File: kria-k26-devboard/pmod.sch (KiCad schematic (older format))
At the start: 6 parts

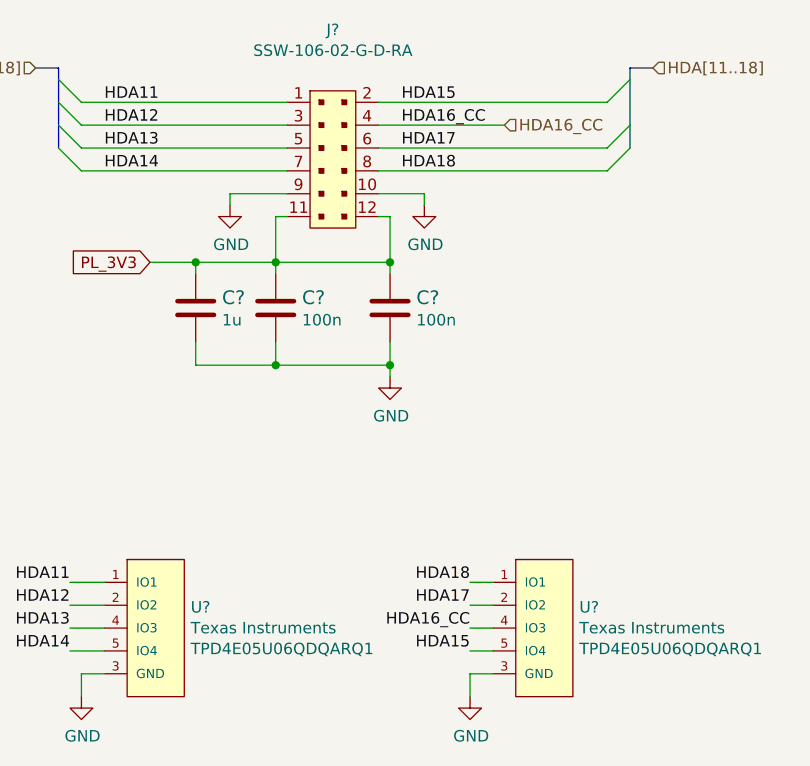
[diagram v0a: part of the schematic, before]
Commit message: Added second ETH interface, connect POE PSE
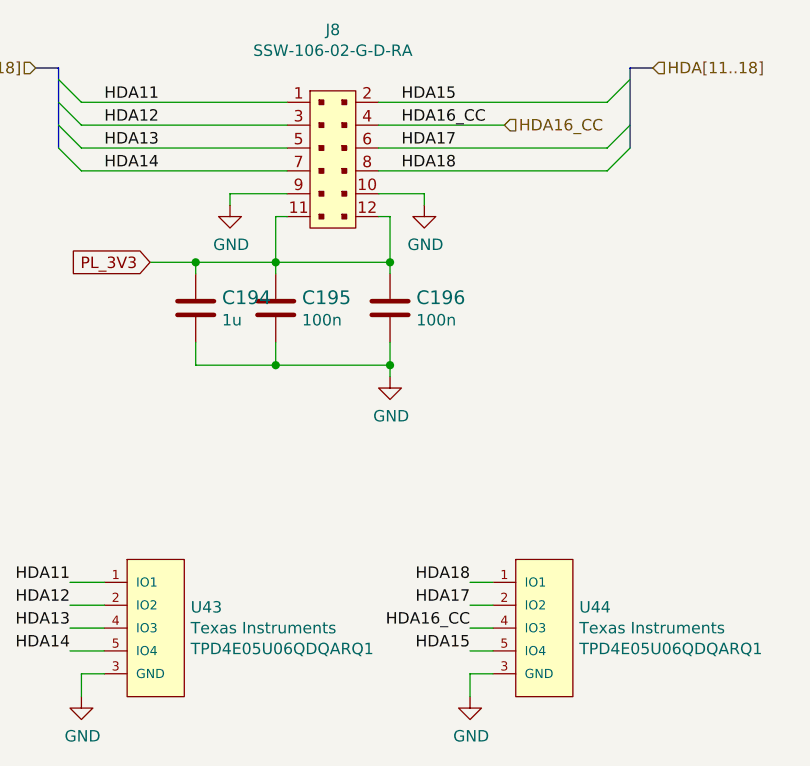
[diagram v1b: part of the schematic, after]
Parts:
- gave numbers to parts that had none: 6
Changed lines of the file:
@@
 $EndDescr
 $Comp
-L antmicroTVSDiodes:TPD4E05U06QDQARQ1 U?
+L antmicroTVSDiodes:TPD4E05U06QDQARQ1 U43
 U 1 1 6498DC0A
 P 4600 5050
-F 0 "U?" H 4928 5141 50  0000 L CNN
+F 0 "U43" H 4928 5141 50  0000 L CNN
 F 1 "TPD4E05U06QDQARQ1" H 4650 4650 50  0001 L CNN
 F 2 "antmicro-footprints:TPD4E05U06QDQARQ1" H 4650 5500 50  0001 L CNN
@@
 $EndComp
 $Comp
-L antmicroRectangularConnectorsHeadersFemalePins:SSW-106-02-G-D-RA J?
+L antmicroRectangularConnectorsHeadersFemalePins:SSW-106-02-G-D-RA J8
 U 1 1 649925B1
 P 5550 3000
-F 0 "J?" H 5550 3567 50  0000 C CNN
+F 0 "J8" H 5550 3567 50  0000 C CNN
 F 1 "SSW-106-02-G-D-RA" H 5550 3476 50  0000 C CNN
 F 2 "antmicro-footprints:SAMTEC_SSW-106-02-G-D-RA" H 5150 3550 50  0001 L BNN
@@
 	5100 3150 5100 3200
 $Comp
-L power:GND #PWR?
+L power:GND #PWR0329
 U 1 1 649A6690
 P 4450 5350
-F 0 "#PWR?" H 4450 5100 50  0001 C CNN
+F 0 "#PWR0329" H 4450 5100 50  0001 C CNN
 F 1 "GND" H 4455 5177 50  0000 C CNN
 F 2 "" H 4450 5350 50  0001 C CNN
@@
 	4450 5250 4550 5250
 $Comp
-L power:GND #PWR?
+L power:GND #PWR0330
 U 1 1 649A6F75
 P 5100 3200
-F 0 "#PWR?" H 5100 2950 50  0001 C CNN
+F 0 "#PWR0330" H 5100 2950 50  0001 C CNN
 F 1 "GND" H 5105 3027 50  0000 C CNN
 F 2 "" H 5100 3200 50  0001 C CNN
@@
 $EndComp
 $Comp
-L power:GND #PWR?
+L power:GND #PWR0331
 U 1 1 649A7323
 P 5950 3200
-F 0 "#PWR?" H 5950 2950 50  0001 C CNN
+F 0 "#PWR0331" H 5950 2950 50  0001 C CNN
 F 1 "GND" H 5955 3027 50  0000 C CNN
 F 2 "" H 5950 3200 50  0001 C CNN
@@
 	6250 5050 6150 5050
 $Comp
-L antmicroTVSDiodes:TPD4E05U06QDQARQ1 U?
+L antmicroTVSDiodes:TPD4E05U06QDQARQ1 U44
 U 1 1 649B0170
 P 6300 5050
-F 0 "U?" H 6628 5141 50  0000 L CNN
+F 0 "U44" H 6628 5141 50  0000 L CNN
 F 1 "TPD4E05U06QDQARQ1" H 6350 4650 50  0001 L CNN
 F 2 "antmicro-footprints:TPD4E05U06QDQARQ1" H 6350 5500 50  0001 L CNN
@@
 	6150 5150 6250 5150
 $Comp
-L power:GND #PWR?
+L power:GND #PWR0332
 U 1 1 649B2E10
 P 6150 5350
-F 0 "#PWR?" H 6150 5100 50  0001 C CNN
+F 0 "#PWR0332" H 6150 5100 50  0001 C CNN
 F 1 "GND" H 6155 5177 50  0000 C CNN
 F 2 "" H 6150 5350 50  0001 C CNN
@@
 PL_3V3
 $Comp
-L antmicroCapacitors0402:C_100n_0402 C?
+L antmicroCapacitors0402:C_100n_0402 C195
 U 1 1 649C2025
 P 5300 3650
-F 0 "C?" H 5415 3695 60  0000 L CNN
+F 0 "C195" H 5415 3695 60  0000 L CNN
 F 1 "C_100n_0402" H 5300 3500 60  0001 C CNN
 F 2 "antmicro-footprints:0402-cap" H 5500 3850 60  0001 L CNN
@@
 $EndComp
 $Comp
-L antmicroCapacitors0402:C_100n_0402 C?
+L antmicroCapacitors0402:C_100n_0402 C196
 U 1 1 649C25C6
 P 5800 3650
-F 0 "C?" H 5915 3695 60  0000 L CNN
+F 0 "C196" H 5915 3695 60  0000 L CNN
 F 1 "C_100n_0402" H 5800 3500 60  0001 C CNN
 F 2 "antmicro-footprints:0402-cap" H 6000 3850 60  0001 L CNN
@@
 $EndComp
 $Comp
-L antmicroCapacitors0402:C_1u_0402 C?
+L antmicroCapacitors0402:C_1u_0402 C194
 U 1 1 649C4ADC
 P 4950 3650
-F 0 "C?" H 5065 3695 60  0000 L CNN
+F 0 "C194" H 5065 3695 60  0000 L CNN
 F 1 "C_1u_0402" H 4950 3500 60  0001 C CNN
 F 2 "antmicro-footprints:0402-cap" H 5150 3850 60  0001 L CNN
@@
 	4950 3800 4950 3900
 $Comp
-L power:GND #PWR?
+L power:GND #PWR0333
 U 1 1 649DA63B
 P 5800 3950
-F 0 "#PWR?" H 5800 3700 50  0001 C CNN
+F 0 "#PWR0333" H 5800 3700 50  0001 C CNN
 F 1 "GND" H 5805 3777 50  0000 C CNN
 F 2 "" H 5800 3950 50  0001 C CNN

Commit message: Finished tidying up the schematic
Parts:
- added D?: ESD9L5.0ST5G, antmicro-footprints:DIOM1006X40N, symbol antmicroTVSDiodes:ESD9L5.0ST5G
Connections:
- wire segments 40 -> 44
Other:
- note added: "PMOD"
- moved on the sheet: C194
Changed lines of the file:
@@
 $Descr A4 11693 8268
 encoding utf-8
-Sheet 16 19
+Sheet 8 19
 Title ""
 Date ""
@@
 Wire Wire Line
 	5350 3250 5300 3250
-Text GLabel 4750 3450 0    50   Input ~ 0
+Text GLabel 3900 3450 0    50   Input ~ 0
 PL_3V3
 $Comp
@@
 L antmicroCapacitors0402:C_1u_0402 C194
 U 1 1 649C4ADC
-P 4950 3650
-F 0 "C194" H 5065 3695 60  0000 L CNN
-F 1 "C_1u_0402" H 4950 3500 60  0001 C CNN
-F 2 "antmicro-footprints:0402-cap" H 5150 3850 60  0001 L CNN
-F 3 "" H 4950 3650 50  0001 C CNN
-F 4 "TDK" H 5150 4050 60  0001 L CNN "Manufacturer"
-F 5 "C1005X6S1A105K050BC" H 5150 3950 60  0001 L CNN "MPN"
-F 6 "1u" H 5065 3597 50  0000 L CNN "Val"
-	1    4950 3650
-	1    0    0    -1
-$EndComp
-Wire Wire Line
-	4950 3500 4950 3450
+P 4800 3650
+F 0 "C194" H 4915 3695 60  0000 L CNN
+F 1 "C_1u_0402" H 4800 3500 60  0001 C CNN
+F 2 "antmicro-footprints:0402-cap" H 5000 3850 60  0001 L CNN
+F 3 "" H 4800 3650 50  0001 C CNN
+F 4 "TDK" H 5000 4050 60  0001 L CNN "Manufacturer"
+F 5 "C1005X6S1A105K050BC" H 5000 3950 60  0001 L CNN "MPN"
+F 6 "1u" H 4915 3597 50  0000 L CNN "Val"
+	1    4800 3650
+	1    0    0    -1
+$EndComp
+Wire Wire Line
+	4800 3500 4800 3450
 Wire Wire Line
 	5750 3250 5800 3250
 Wire Wire Line
 	5300 3250 5300 3450
-Wire Wire Line
-	4750 3450 4950 3450
-Connection ~ 4950 3450
-Wire Wire Line
-	4950 3800 4950 3900
+Connection ~ 4800 3450
 $Comp
 L power:GND #PWR0333
 U 1 1 649DA63B
-P 5800 3950
-F 0 "#PWR0333" H 5800 3700 50  0001 C CNN
-F 1 "GND" H 5805 3777 50  0000 C CNN
-F 2 "" H 5800 3950 50  0001 C CNN
-F 3 "" H 5800 3950 50  0001 C CNN
-	1    5800 3950
+P 5800 4150
+F 0 "#PWR0333" H 5800 3900 50  0001 C CNN
+F 1 "GND" H 5805 3977 50  0000 C CNN
+F 2 "" H 5800 4150 50  0001 C CNN
+F 3 "" H 5800 4150 50  0001 C CNN
+	1    5800 4150
 	1    0    0    -1
 $EndComp
@@
 	5800 3450 5800 3500
 Wire Wire Line
-	5800 3900 5800 3800
-Wire Wire Line
 	5300 3500 5300 3450
-Wire Wire Line
-	5300 3800 5300 3900
-Connection ~ 5300 3900
-Wire Wire Line
-	5300 3900 5800 3900
-Wire Wire Line
-	5800 3950 5800 3900
-Connection ~ 5800 3900
-Wire Wire Line
-	4950 3900 5300 3900
-Wire Wire Line
-	4950 3450 5300 3450
+Connection ~ 5300 4100
+Wire Wire Line
+	5300 4100 5800 4100
+Wire Wire Line
+	4800 4100 5300 4100
+Wire Wire Line
+	4800 3450 5300 3450
+Text Notes 550  750  0    100  ~ 20
+PMOD
+$Comp
+L antmicroTVSDiodes:ESD9L5.0ST5G D?
+U 1 1 69767A1C
+P 4050 3750
+F 0 "D?" V 4096 3650 50  0000 R CNN
+F 1 "ESD9L5.0ST5G" V 4005 3650 50  0000 R CNN
+F 2 "antmicro-footprints:DIOM1006X40N" H 3800 3950 50  0001 C CNN
+F 3 "https://www.farnell.com/datasheets/2353986.pdf" H 4050 3750 50  0001 C CNN
+F 4 "ESD9L5.0ST5G" H 3750 4000 50  0001 C CNN "MPN"
+F 5 "ONSEMI" H 4200 4000 50  0001 C CNN "Manufacturer"
+	1    4050 3750
+	0    -1   -1   0
+$EndComp
+Wire Wire Line
+	3900 3450 4050 3450
+Wire Wire Line
+	4800 4100 4050 4100
+Wire Wire Line
+	4050 4100 4050 4000
+Wire Wire Line
+	4050 3500 4050 3450
+Connection ~ 4050 3450
+Wire Wire Line
+	4050 3450 4800 3450
+Wire Wire Line
+	4800 3800 4800 4100
+Wire Wire Line
+	5800 4150 5800 4100
+Wire Wire Line
+	5800 3800 5800 4100
+Connection ~ 5800 4100
+Wire Wire Line
+	5300 3800 5300 4100
+Connection ~ 4800 4100
 Wire Bus Line
 	6850 2600 6850 2950

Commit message: Initial placement of power supply
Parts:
- removed D?: ESD9L5.0ST5G, antmicro-footprints:DIOM1006X40N, symbol antmicroTVSDiodes:ESD9L5.0ST5G
- added D3: PTVS5V0Z1USKPYL, antmicro-footprints:SOD-964, symbol antmicroTVSDiodes:PTVS5V0Z1USKPYL
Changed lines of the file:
@@
 Text Notes 550  750  0    100  ~ 20
 PMOD
-$Comp
-L antmicroTVSDiodes:ESD9L5.0ST5G D?
-U 1 1 69767A1C
-P 4050 3750
-F 0 "D?" V 4096 3650 50  0000 R CNN
-F 1 "ESD9L5.0ST5G" V 4005 3650 50  0000 R CNN
-F 2 "antmicro-footprints:DIOM1006X40N" H 3800 3950 50  0001 C CNN
-F 3 "https://www.farnell.com/datasheets/2353986.pdf" H 4050 3750 50  0001 C CNN
-F 4 "ESD9L5.0ST5G" H 3750 4000 50  0001 C CNN "MPN"
-F 5 "ONSEMI" H 4200 4000 50  0001 C CNN "Manufacturer"
-	1    4050 3750
-	0    -1   -1   0
-$EndComp
 Wire Wire Line
 	3900 3450 4050 3450
 Wire Wire Line
 	4800 4100 4050 4100
-Wire Wire Line
-	4050 4100 4050 4000
-Wire Wire Line
-	4050 3500 4050 3450
 Connection ~ 4050 3450
 Wire Wire Line
@@
 	5300 3800 5300 4100
 Connection ~ 4800 4100
+$Comp
+L antmicroTVSDiodes:PTVS5V0Z1USKPYL D3
+U 1 1 69B7F430
+P 4050 3750
+F 0 "D3" V 4103 3622 60  0000 R CNN
+F 1 "PTVS5V0Z1USKPYL" H 4250 3950 60  0000 R CNN
+F 2 "antmicro-footprints:SOD-964" H 4250 3950 60  0001 L CNN
+F 3 "https://pl.mouser.com/datasheet/2/916/PTVS5V0Z1USKP-1600477.pdf" H 4250 4050 60  0001 L CNN
+F 4 "Nexperia" H 4250 4850 60  0001 L CNN "Manufacturer"
+F 5 "PTVS5V0Z1USKPYL" H 4250 4250 60  0001 L CNN "MPN"
+	1    4050 3750
+	0    -1   -1   0
+$EndComp
+Wire Wire Line
+	4050 3450 4050 3550
+Wire Wire Line
+	4050 3950 4050 4100
 Wire Bus Line
 	6850 2600 6850 2950

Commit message: Progress in PCB placement
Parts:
- renumbered C194 to C39, C195 to C40, C196 to C41, J8 to J4, U43 to U12, U44 to U13
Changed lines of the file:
@@
 $EndDescr
 $Comp
-L antmicroTVSDiodes:TPD4E05U06QDQARQ1 U43
+L antmicroTVSDiodes:TPD4E05U06QDQARQ1 U12
 U 1 1 6498DC0A
 P 4600 5050
-F 0 "U43" H 4928 5141 50  0000 L CNN
+F 0 "U12" H 4928 5141 50  0000 L CNN
 F 1 "TPD4E05U06QDQARQ1" H 4650 4650 50  0001 L CNN
 F 2 "antmicro-footprints:TPD4E05U06QDQARQ1" H 4650 5500 50  0001 L CNN
@@
 $EndComp
 $Comp
-L antmicroRectangularConnectorsHeadersFemalePins:SSW-106-02-G-D-RA J8
+L antmicroRectangularConnectorsHeadersFemalePins:SSW-106-02-G-D-RA J4
 U 1 1 649925B1
 P 5550 3000
-F 0 "J8" H 5550 3567 50  0000 C CNN
+F 0 "J4" H 5550 3567 50  0000 C CNN
 F 1 "SSW-106-02-G-D-RA" H 5550 3476 50  0000 C CNN
 F 2 "antmicro-footprints:SAMTEC_SSW-106-02-G-D-RA" H 5150 3550 50  0001 L BNN
@@
 	5100 3150 5100 3200
 $Comp
-L power:GND #PWR0329
+L power:GND #PWR062
 U 1 1 649A6690
 P 4450 5350
-F 0 "#PWR0329" H 4450 5100 50  0001 C CNN
+F 0 "#PWR062" H 4450 5100 50  0001 C CNN
 F 1 "GND" H 4455 5177 50  0000 C CNN
 F 2 "" H 4450 5350 50  0001 C CNN
@@
 	4450 5250 4550 5250
 $Comp
-L power:GND #PWR0330
+L power:GND #PWR063
 U 1 1 649A6F75
 P 5100 3200
-F 0 "#PWR0330" H 5100 2950 50  0001 C CNN
+F 0 "#PWR063" H 5100 2950 50  0001 C CNN
 F 1 "GND" H 5105 3027 50  0000 C CNN
 F 2 "" H 5100 3200 50  0001 C CNN
@@
 $EndComp
 $Comp
-L power:GND #PWR0331
+L power:GND #PWR065
 U 1 1 649A7323
 P 5950 3200
-F 0 "#PWR0331" H 5950 2950 50  0001 C CNN
+F 0 "#PWR065" H 5950 2950 50  0001 C CNN
 F 1 "GND" H 5955 3027 50  0000 C CNN
 F 2 "" H 5950 3200 50  0001 C CNN
@@
 	6250 5050 6150 5050
 $Comp
-L antmicroTVSDiodes:TPD4E05U06QDQARQ1 U44
+L antmicroTVSDiodes:TPD4E05U06QDQARQ1 U13
 U 1 1 649B0170
 P 6300 5050
-F 0 "U44" H 6628 5141 50  0000 L CNN
+F 0 "U13" H 6628 5141 50  0000 L CNN
 F 1 "TPD4E05U06QDQARQ1" H 6350 4650 50  0001 L CNN
 F 2 "antmicro-footprints:TPD4E05U06QDQARQ1" H 6350 5500 50  0001 L CNN
@@
 	6150 5150 6250 5150
 $Comp
-L power:GND #PWR0332
+L power:GND #PWR066
 U 1 1 649B2E10
 P 6150 5350
-F 0 "#PWR0332" H 6150 5100 50  0001 C CNN
+F 0 "#PWR066" H 6150 5100 50  0001 C CNN
 F 1 "GND" H 6155 5177 50  0000 C CNN
 F 2 "" H 6150 5350 50  0001 C CNN
@@
 PL_3V3
 $Comp
-L antmicroCapacitors0402:C_100n_0402 C195
+L antmicroCapacitors0402:C_100n_0402 C40
 U 1 1 649C2025
 P 5300 3650
-F 0 "C195" H 5415 3695 60  0000 L CNN
+F 0 "C40" H 5415 3695 60  0000 L CNN
 F 1 "C_100n_0402" H 5300 3500 60  0001 C CNN
 F 2 "antmicro-footprints:0402-cap" H 5500 3850 60  0001 L CNN
@@
 $EndComp
 $Comp
-L antmicroCapacitors0402:C_100n_0402 C196
+L antmicroCapacitors0402:C_100n_0402 C41
 U 1 1 649C25C6
 P 5800 3650
-F 0 "C196" H 5915 3695 60  0000 L CNN
+F 0 "C41" H 5915 3695 60  0000 L CNN
 F 1 "C_100n_0402" H 5800 3500 60  0001 C CNN
 F 2 "antmicro-footprints:0402-cap" H 6000 3850 60  0001 L CNN
@@
 $EndComp
 $Comp
-L antmicroCapacitors0402:C_1u_0402 C194
+L antmicroCapacitors0402:C_1u_0402 C39
 U 1 1 649C4ADC
 P 4800 3650
-F 0 "C194" H 4915 3695 60  0000 L CNN
+F 0 "C39" H 4915 3695 60  0000 L CNN
 F 1 "C_1u_0402" H 4800 3500 60  0001 C CNN
 F 2 "antmicro-footprints:0402-cap" H 5000 3850 60  0001 L CNN
@@
 Connection ~ 4800 3450
 $Comp
-L power:GND #PWR0333
+L power:GND #PWR064
 U 1 1 649DA63B
 P 5800 4150
-F 0 "#PWR0333" H 5800 3900 50  0001 C CNN
+F 0 "#PWR064" H 5800 3900 50  0001 C CNN
 F 1 "GND" H 5805 3977 50  0000 C CNN
 F 2 "" H 5800 4150 50  0001 C CNN

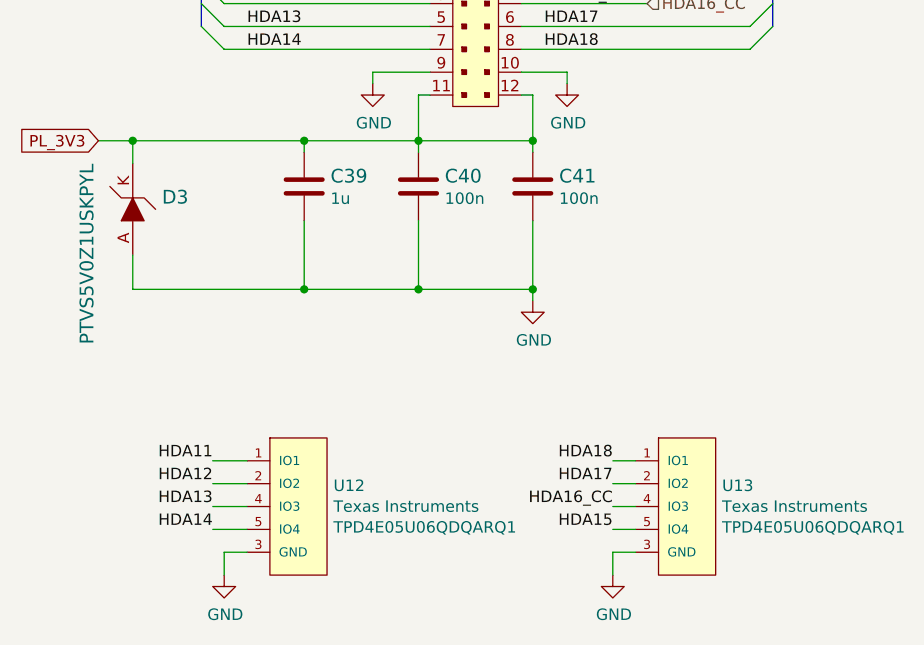
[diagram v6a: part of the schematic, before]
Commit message: Fixed missing USB - M2 connection, finishing touches of PCB
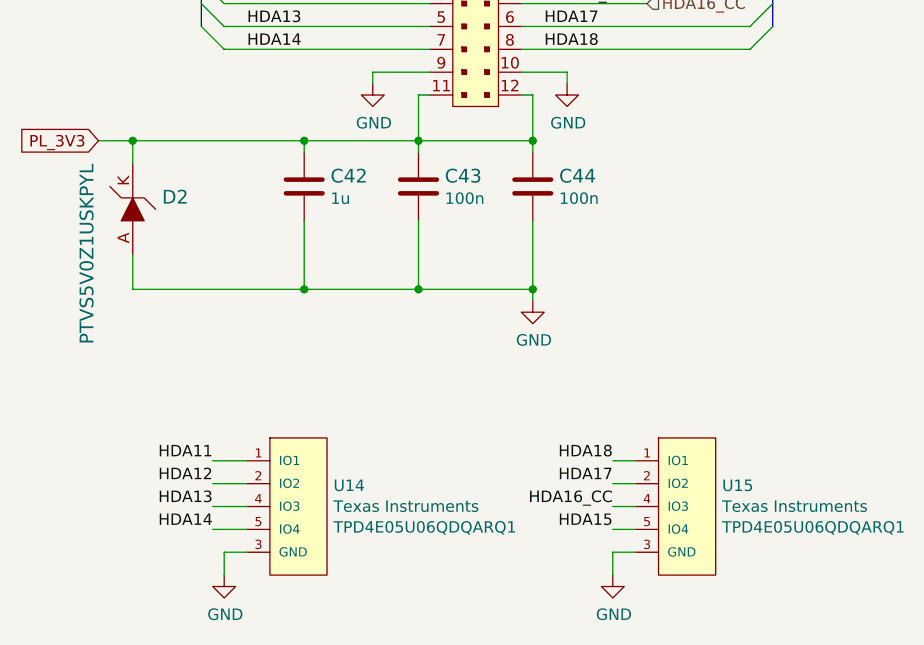
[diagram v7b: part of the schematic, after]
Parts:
- renumbered C39 to C42, C40 to C43, C41 to C44, D3 to D2, U12 to U14, U13 to U15
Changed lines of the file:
@@
 $EndDescr
 $Comp
-L antmicroTVSDiodes:TPD4E05U06QDQARQ1 U12
+L antmicroTVSDiodes:TPD4E05U06QDQARQ1 U14
 U 1 1 6498DC0A
 P 4600 5050
-F 0 "U12" H 4928 5141 50  0000 L CNN
+F 0 "U14" H 4928 5141 50  0000 L CNN
 F 1 "TPD4E05U06QDQARQ1" H 4650 4650 50  0001 L CNN
 F 2 "antmicro-footprints:TPD4E05U06QDQARQ1" H 4650 5500 50  0001 L CNN
@@
 	5100 3150 5100 3200
 $Comp
-L power:GND #PWR062
+L power:GND #PWR068
 U 1 1 649A6690
 P 4450 5350
-F 0 "#PWR062" H 4450 5100 50  0001 C CNN
+F 0 "#PWR068" H 4450 5100 50  0001 C CNN
 F 1 "GND" H 4455 5177 50  0000 C CNN
 F 2 "" H 4450 5350 50  0001 C CNN
@@
 	4450 5250 4550 5250
 $Comp
-L power:GND #PWR063
+L power:GND #PWR069
 U 1 1 649A6F75
 P 5100 3200
-F 0 "#PWR063" H 5100 2950 50  0001 C CNN
+F 0 "#PWR069" H 5100 2950 50  0001 C CNN
 F 1 "GND" H 5105 3027 50  0000 C CNN
 F 2 "" H 5100 3200 50  0001 C CNN
@@
 $EndComp
 $Comp
-L power:GND #PWR065
+L power:GND #PWR071
 U 1 1 649A7323
 P 5950 3200
-F 0 "#PWR065" H 5950 2950 50  0001 C CNN
+F 0 "#PWR071" H 5950 2950 50  0001 C CNN
 F 1 "GND" H 5955 3027 50  0000 C CNN
 F 2 "" H 5950 3200 50  0001 C CNN
@@
 	6250 5050 6150 5050
 $Comp
-L antmicroTVSDiodes:TPD4E05U06QDQARQ1 U13
+L antmicroTVSDiodes:TPD4E05U06QDQARQ1 U15
 U 1 1 649B0170
 P 6300 5050
-F 0 "U13" H 6628 5141 50  0000 L CNN
+F 0 "U15" H 6628 5141 50  0000 L CNN
 F 1 "TPD4E05U06QDQARQ1" H 6350 4650 50  0001 L CNN
 F 2 "antmicro-footprints:TPD4E05U06QDQARQ1" H 6350 5500 50  0001 L CNN
@@
 	6150 5150 6250 5150
 $Comp
-L power:GND #PWR066
+L power:GND #PWR072
 U 1 1 649B2E10
 P 6150 5350
-F 0 "#PWR066" H 6150 5100 50  0001 C CNN
+F 0 "#PWR072" H 6150 5100 50  0001 C CNN
 F 1 "GND" H 6155 5177 50  0000 C CNN
 F 2 "" H 6150 5350 50  0001 C CNN
@@
 PL_3V3
 $Comp
-L antmicroCapacitors0402:C_100n_0402 C40
+L antmicroCapacitors0402:C_100n_0402 C43
 U 1 1 649C2025
 P 5300 3650
-F 0 "C40" H 5415 3695 60  0000 L CNN
+F 0 "C43" H 5415 3695 60  0000 L CNN
 F 1 "C_100n_0402" H 5300 3500 60  0001 C CNN
 F 2 "antmicro-footprints:0402-cap" H 5500 3850 60  0001 L CNN
@@
 $EndComp
 $Comp
-L antmicroCapacitors0402:C_100n_0402 C41
+L antmicroCapacitors0402:C_100n_0402 C44
 U 1 1 649C25C6
 P 5800 3650
-F 0 "C41" H 5915 3695 60  0000 L CNN
+F 0 "C44" H 5915 3695 60  0000 L CNN
 F 1 "C_100n_0402" H 5800 3500 60  0001 C CNN
 F 2 "antmicro-footprints:0402-cap" H 6000 3850 60  0001 L CNN
@@
 $EndComp
 $Comp
-L antmicroCapacitors0402:C_1u_0402 C39
+L antmicroCapacitors0402:C_1u_0402 C42
 U 1 1 649C4ADC
 P 4800 3650
-F 0 "C39" H 4915 3695 60  0000 L CNN
+F 0 "C42" H 4915 3695 60  0000 L CNN
 F 1 "C_1u_0402" H 4800 3500 60  0001 C CNN
 F 2 "antmicro-footprints:0402-cap" H 5000 3850 60  0001 L CNN
@@
 Connection ~ 4800 3450
 $Comp
-L power:GND #PWR064
+L power:GND #PWR070
 U 1 1 649DA63B
 P 5800 4150
-F 0 "#PWR064" H 5800 3900 50  0001 C CNN
+F 0 "#PWR070" H 5800 3900 50  0001 C CNN
 F 1 "GND" H 5805 3977 50  0000 C CNN
 F 2 "" H 5800 4150 50  0001 C CNN
@@
 Connection ~ 4800 4100
 $Comp
-L antmicroTVSDiodes:PTVS5V0Z1USKPYL D3
+L antmicroTVSDiodes:PTVS5V0Z1USKPYL D2
 U 1 1 69B7F430
 P 4050 3750
-F 0 "D3" V 4103 3622 60  0000 R CNN
+F 0 "D2" V 4103 3622 60  0000 R CNN
 F 1 "PTVS5V0Z1USKPYL" H 4250 3950 60  0000 R CNN
 F 2 "antmicro-footprints:SOD-964" H 4250 3950 60  0001 L CNN
